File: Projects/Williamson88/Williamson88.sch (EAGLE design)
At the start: 1 part

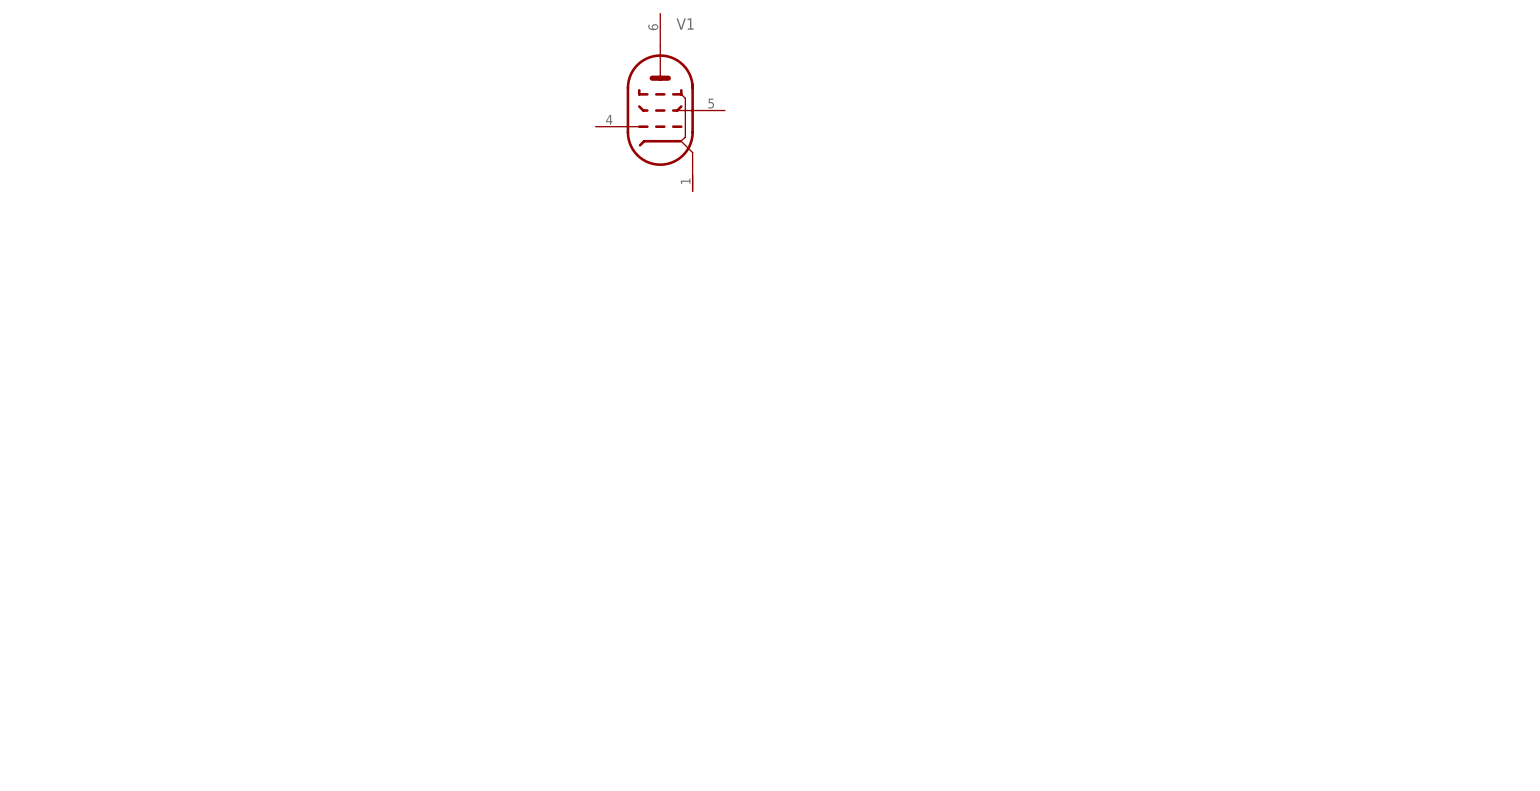
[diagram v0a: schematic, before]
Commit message: Created schematic and first placement
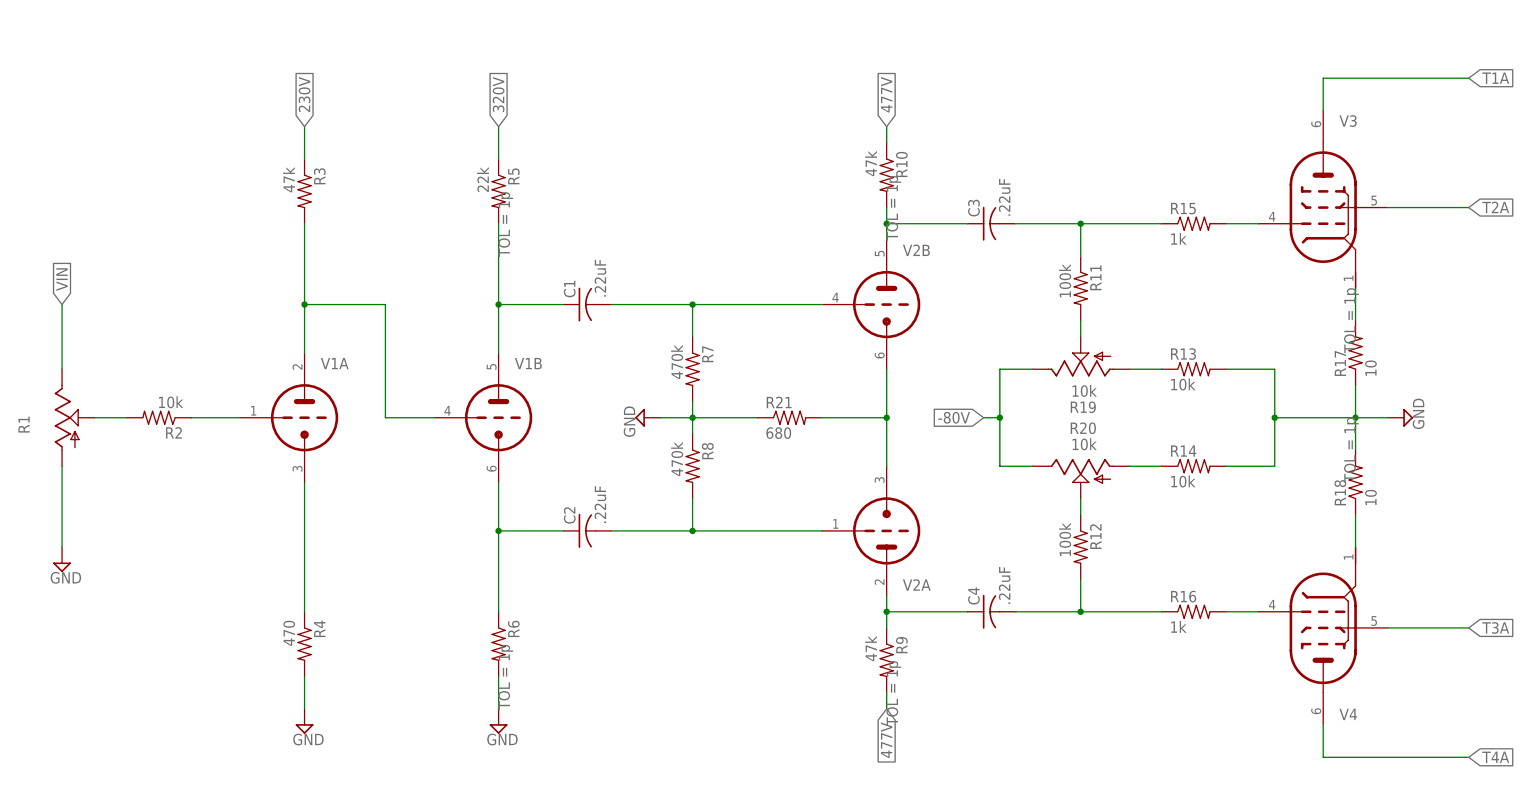
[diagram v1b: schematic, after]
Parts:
- added C1, C2, C3, C4: .22uF, rcl:C-US150-091X182
- added R1: (no value), pot:TRIM_US-B25P
- added R10, R3, R9: 47k, rcl:R-US_0309/10
- added R11, R12: 100k, rcl:R-US_0309/10
- added R13, R14, R2: 10k, rcl:R-US_0309/10
- added R15, R16: 1k, rcl:R-US_0309/10
- added R17, R18: 10, rcl:R-US_0309/10
- added R19, R20: 10k, pot:TRIM_US-B25P
- added R21: 680, rcl:R-US_0309/10
- added R4: 470, rcl:R-US_0309/10
- added R5: 22k, rcl:R-US_0309/10
- added R6: (no value), rcl:R-US_0309/10
- added R7, R8: 470k, rcl:R-US_0309/10
- added V2: (no value), tubes:6SN7GT-P
- added V3, V4: (no value), tubes:KT88-P
- V1: device tubes:KT88-P -> tubes:6SN7GT-P
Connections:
- new net -80V: R19.E, R20.E
- new net 230V: R3.1
- new net 320V: R5.1
- new net 477V: R10.1, R9.2
- new net GND: R1.A, R13.2, R14.2, R17.1, R18.2, R21.1, R4.2, R6.2, R7.2, R8.1
- new net N$1: R3.2, V1A.TA, V1B.TG
- new net N$10: C3.1, R10.2, V2B.TA
- new net N$11: C4.1, R9.1, V2A.TA
- new net N$12: C3.2, R11.1, R15.1
- new net N$13: R15.2, V3G$1.PG
- new net N$14: C4.2, R12.2, R16.1
- new net N$15: R16.2, V4G$1.PG
- new net N$16: R17.2, V3G$1.PK
- new net N$17: R18.1, V4G$1.PK
- new net N$18: R13.1, R19.A
- new net N$19: R2.1, V1A.TG
- new net N$2: R4.1, V1A.TK
- new net N$20: R14.1, R20.A
- new net N$21: R12.1, R20.S
- new net N$22: R11.2, R19.S
- new net N$3: C2.1, R6.1, V1B.TK
- new net N$4: C1.1, R5.2, V1B.TA
- new net N$6: C1.2, R7.1, V2B.TG
- new net N$7: C2.2, R8.2, V2A.TG
- new net N$8: R1.S, R2.2
- new net N$9: R21.2, V2A.TK, V2B.TK
- new net T1A: V3G$1.PA
- new net T2A: V3G$1.PSG
- new net T3A: V4G$1.PSG
- new net T4A: V4G$1.PA
- new net VIN: R1.E
